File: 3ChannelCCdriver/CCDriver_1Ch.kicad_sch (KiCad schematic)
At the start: 5 parts, among them U1 AL8860WT-7

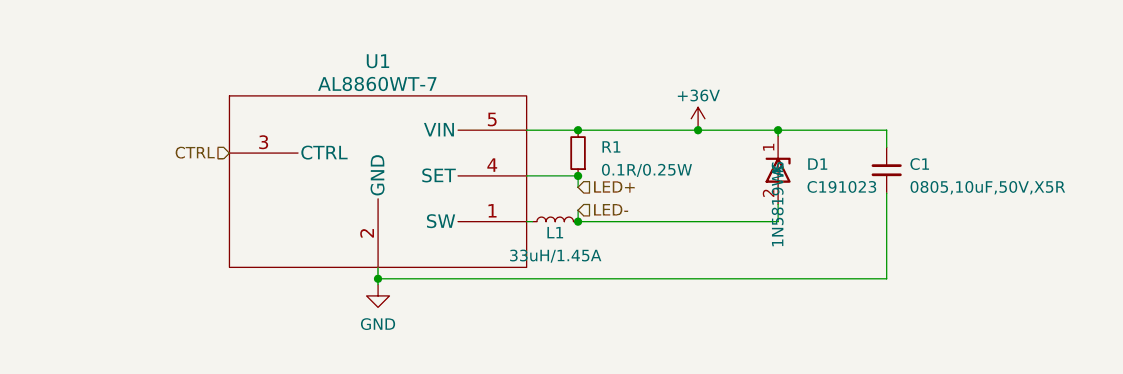
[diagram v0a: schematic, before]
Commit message: Changed rev to B01
Changed diode pinout on CC driver
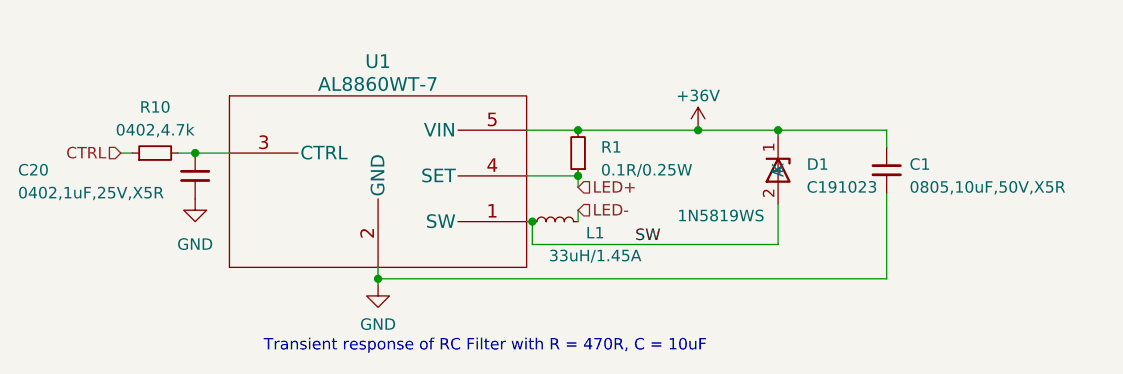
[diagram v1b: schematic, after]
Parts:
- added C20: 0402,1uF,25V,X5R, C_0402_1005Metric, symbol jlcpcb-basic-capacitor:0402,1uF,25V,X5R
- added R10: 0402,4.7k, R_0402_1005Metric, symbol jlcpcb-basic-resistor:0402,4.7k
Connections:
- net CTRL: now also R10.1; no longer U1.3 (CTRL)
- net GND: now also C20.2
- net LED-: no longer D1.2 (A)
- net SW: now reaches L1.1, U1.1 (SW)
- net SW: now also D1.2 (A)
- new net: C20.1, R10.2, U1.3 (CTRL)
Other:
- note added: "Transient response of RC Filter with R = 470R, C = 10uF"

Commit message: neat-ified schematics
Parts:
- D1: footprint Diode_SMD:D_SOD-323 -> Diode_SMD:D_SMA; LCSC C191023 -> C8678
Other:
- note added: "LED Driver, set to 1A with Rs=0.1R"
- note removed: "Transient response of RC Filter with R = 470R, C = 10uF"
- title: (none) -> 1 Ch CC LED Driver
- moved on the sheet: L1, R1
